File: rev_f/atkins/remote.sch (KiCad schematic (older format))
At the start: 21 parts, among them J1 Conn_01x18_Female, J11 BME390, J2 Conn_01x18_Female, J3 Conn_01x15_Female, J4 Conn_01x03_Female, J5 Conn_01x04_Female, J9 SCD30, SW1 SW_Push, SW2 SW_Push

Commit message: update
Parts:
- removed J3: Conn_01x15_Female, Connector_PinSocket_2.54mm:PinSocket_1x15_P2.54mm_Vertical, symbol Connector:Conn_01x15_Female
- added J3: Conn_01x14_Female, Connector_PinSocket_2.54mm:PinSocket_1x14_P2.54mm_Vertical, symbol Connector:Conn_01x14_Female
- added J8, J?: Conn_01x04_Female, Connector_PinSocket_2.54mm:PinSocket_1x04_P2.54mm_Vertical, symbol Connector:Conn_01x04_Female
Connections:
- net +3V3: now also J3.3 (Pin_3), J3.7 (Pin_7), J8.2 (Pin_2), J?.2 (Pin_2)
- net 34_A6: now also J3.13 (Pin_13)
- net 35_A7: now also J3.14 (Pin_14)
- net 36_A0: now also J3.9 (Pin_9)
- net 37_A1: now also J3.10 (Pin_10)
- net 38_A2: now also J3.11 (Pin_11)
- net 39_A3: now also J3.12 (Pin_12)
- net GND: now also J3.2 (Pin_2), J3.6 (Pin_6), J3.8 (Pin_8), J8.1 (Pin_1), J?.1 (Pin_1)
- net RX: now also J3.4 (Pin_4)
- net SCL: now also J8.4 (Pin_4), J?.4 (Pin_4)
- net SDA: now also J8.3 (Pin_3), J?.3 (Pin_3)
- net TX: now also J3.5 (Pin_5)
- new net VUSB: J3.1 (Pin_1)
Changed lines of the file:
@@
 Text GLabel 3150 2000 0    50   Input ~ 0
 RST
-Text GLabel 6950 3100 0    50   Input ~ 0
-SCL
-Text GLabel 6950 3200 0    50   Input ~ 0
-SDA
 Text GLabel 6950 3400 0    50   Input ~ 0
 36_A0
@@
 Text GLabel 6950 3700 0    50   Input ~ 0
 39_A3
-Text GLabel 6950 2700 0    50   Input ~ 0
+Text GLabel 6950 2900 0    50   Input ~ 0
 RX
-Text GLabel 6950 2800 0    50   Input ~ 0
+Text GLabel 6950 3000 0    50   Input ~ 0
 TX
 $Comp
@@
 L power:GND #PWR0101
 U 1 1 5FD6AB8A
-P 6675 2600
-F 0 "#PWR0101" H 6675 2350 50  0001 C CNN
-F 1 "GND" H 6680 2427 50  0000 C CNN
-F 2 "" H 6675 2600 50  0001 C CNN
-F 3 "" H 6675 2600 50  0001 C CNN
-	1    6675 2600
+P 6675 2700
+F 0 "#PWR0101" H 6675 2450 50  0001 C CNN
+F 1 "GND" H 6680 2527 50  0000 C CNN
+F 2 "" H 6675 2700 50  0001 C CNN
+F 3 "" H 6675 2700 50  0001 C CNN
+	1    6675 2700
 	0    1    1    0
 $EndComp
@@
 L power:+3V3 #PWR0105
 U 1 1 5FD6C458
-P 6950 2500
-F 0 "#PWR0105" H 6950 2350 50  0001 C CNN
-F 1 "+3V3" H 6925 2675 50  0000 C CNN
-F 2 "" H 6950 2500 50  0001 C CNN
-F 3 "" H 6950 2500 50  0001 C CNN
-	1    6950 2500
-	0    -1   -1   0
-$EndComp
-$Comp
-L power:+3V3 #PWR0106
-U 1 1 5FEF6C10
-P 6950 2900
-F 0 "#PWR0106" H 6950 2750 50  0001 C CNN
-F 1 "+3V3" H 6925 3075 50  0000 C CNN
-F 2 "" H 6950 2900 50  0001 C CNN
-F 3 "" H 6950 2900 50  0001 C CNN
-	1    6950 2900
+P 6600 2800
+F 0 "#PWR0105" H 6600 2650 50  0001 C CNN
+F 1 "+3V3" H 6575 2975 50  0000 C CNN
+F 2 "" H 6600 2800 50  0001 C CNN
+F 3 "" H 6600 2800 50  0001 C CNN
+	1    6600 2800
 	0    -1   -1   0
 $EndComp
@@
 L power:GND #PWR0117
 U 1 1 5FEF7025
-P 6675 3000
-F 0 "#PWR0117" H 6675 2750 50  0001 C CNN
-F 1 "GND" H 6680 2827 50  0000 C CNN
-F 2 "" H 6675 3000 50  0001 C CNN
-F 3 "" H 6675 3000 50  0001 C CNN
-	1    6675 3000
+P 6625 3100
+F 0 "#PWR0117" H 6625 2850 50  0001 C CNN
+F 1 "GND" H 6630 2927 50  0000 C CNN
+F 2 "" H 6625 3100 50  0001 C CNN
+F 3 "" H 6625 3100 50  0001 C CNN
+	1    6625 3100
 	0    1    1    0
-$EndComp
-Wire Wire Line
-	6950 2600 6675 2600
-Wire Wire Line
-	6950 3000 6675 3000
-$Comp
-L Connector:Conn_01x15_Female J3
-U 1 1 5FEFD935
-P 7150 3200
-F 0 "J3" H 7178 3226 50  0000 L CNN
-F 1 "Conn_01x15_Female" H 7178 3135 50  0000 L CNN
-F 2 "Connector_PinSocket_2.54mm:PinSocket_1x15_P2.54mm_Vertical" H 7150 3200 50  0001 C CNN
-F 3 "~" H 7150 3200 50  0001 C CNN
-	1    7150 3200
-	1    0    0    -1
 $EndComp
 $Comp
@@
 Wire Wire Line
 	5525 4300 5150 4300
+$Comp
+L Connector:Conn_01x04_Female J8
+U 1 1 60000D99
+P 8875 3125
+F 0 "J8" H 8903 3101 50  0000 L CNN
+F 1 "Conn_01x04_Female" H 8903 3010 50  0000 L CNN
+F 2 "Connector_PinSocket_2.54mm:PinSocket_1x04_P2.54mm_Vertical" H 8875 3125 50  0001 C CNN
+F 3 "~" H 8875 3125 50  0001 C CNN
+	1    8875 3125
+	1    0    0    -1
+$EndComp
+Text GLabel 8675 3325 0    50   Input ~ 0
+SCL
+Text GLabel 8675 3225 0    50   Input ~ 0
+SDA
+$Comp
+L power:GND #PWR0122
+U 1 1 60000DA1
+P 8300 3025
+F 0 "#PWR0122" H 8300 2775 50  0001 C CNN
+F 1 "GND" H 8305 2852 50  0000 C CNN
+F 2 "" H 8300 3025 50  0001 C CNN
+F 3 "" H 8300 3025 50  0001 C CNN
+	1    8300 3025
+	1    0    0    -1
+$EndComp
+$Comp
+L power:+3V3 #PWR0123
+U 1 1 60000DA7
+P 8550 2950
+F 0 "#PWR0123" H 8550 2800 50  0001 C CNN
+F 1 "+3V3" V 8565 3078 50  0000 L CNN
+F 2 "" H 8550 2950 50  0001 C CNN
+F 3 "" H 8550 2950 50  0001 C CNN
+	1    8550 2950
+	1    0    0    -1
+$EndComp
+Wire Wire Line
+	8675 3125 8550 3125
+Wire Wire Line
+	8550 3125 8550 2950
+Wire Wire Line
+	8675 3025 8300 3025
+Text GLabel 6950 2600 0    50   Input ~ 0
+VUSB
+$Comp
+L power:+3V3 #PWR0106
+U 1 1 6000DA3E
+P 6950 3200
+F 0 "#PWR0106" H 6950 3050 50  0001 C CNN
+F 1 "+3V3" H 6925 3375 50  0000 C CNN
+F 2 "" H 6950 3200 50  0001 C CNN
+F 3 "" H 6950 3200 50  0001 C CNN
+	1    6950 3200
+	0    -1   -1   0
+$EndComp
+$Comp
+L Connector:Conn_01x14_Female J3
+U 1 1 6003FCAE
+P 7150 3200
+F 0 "J3" H 7178 3176 50  0000 L CNN
+F 1 "Conn_01x14_Female" H 7178 3085 50  0000 L CNN
+F 2 "Connector_PinSocket_2.54mm:PinSocket_1x14_P2.54mm_Vertical" H 7150 3200 50  0001 C CNN
+F 3 "~" H 7150 3200 50  0001 C CNN
+	1    7150 3200
+	1    0    0    -1
+$EndComp
+Wire Wire Line
+	6950 2700 6675 2700
+Wire Wire Line
+	6950 2800 6600 2800
+Wire Wire Line
+	6950 3100 6625 3100
+$Comp
+L Connector:Conn_01x04_Female J?
+U 1 1 60065C2D
+P 9450 2200
+F 0 "J?" H 9478 2176 50  0000 L CNN
+F 1 "Conn_01x04_Female" H 9478 2085 50  0000 L CNN
+F 2 "Connector_PinSocket_2.54mm:PinSocket_1x04_P2.54mm_Vertical" H 9450 2200 50  0001 C CNN
+F 3 "~" H 9450 2200 50  0001 C CNN
+	1    9450 2200
+	1    0    0    -1
+$EndComp
+Text GLabel 9250 2400 0    50   Input ~ 0
+SCL
+Text GLabel 9250 2300 0    50   Input ~ 0
+SDA
+$Comp
+L power:GND #PWR?
+U 1 1 60065C39
+P 8875 2100
+F 0 "#PWR?" H 8875 1850 50  0001 C CNN
+F 1 "GND" H 8880 1927 50  0000 C CNN
+F 2 "" H 8875 2100 50  0001 C CNN
+F 3 "" H 8875 2100 50  0001 C CNN
+	1    8875 2100
+	1    0    0    -1
+$EndComp
+$Comp
+L power:+3V3 #PWR?
+U 1 1 60065C43
+P 9125 2025
+F 0 "#PWR?" H 9125 1875 50  0001 C CNN
+F 1 "+3V3" V 9140 2153 50  0000 L CNN
+F 2 "" H 9125 2025 50  0001 C CNN
+F 3 "" H 9125 2025 50  0001 C CNN
+	1    9125 2025
+	1    0    0    -1
+$EndComp
+Wire Wire Line
+	9250 2200 9125 2200
+Wire Wire Line
+	9125 2200 9125 2025
+Wire Wire Line
+	9250 2100 8875 2100
 $EndSCHEMATC

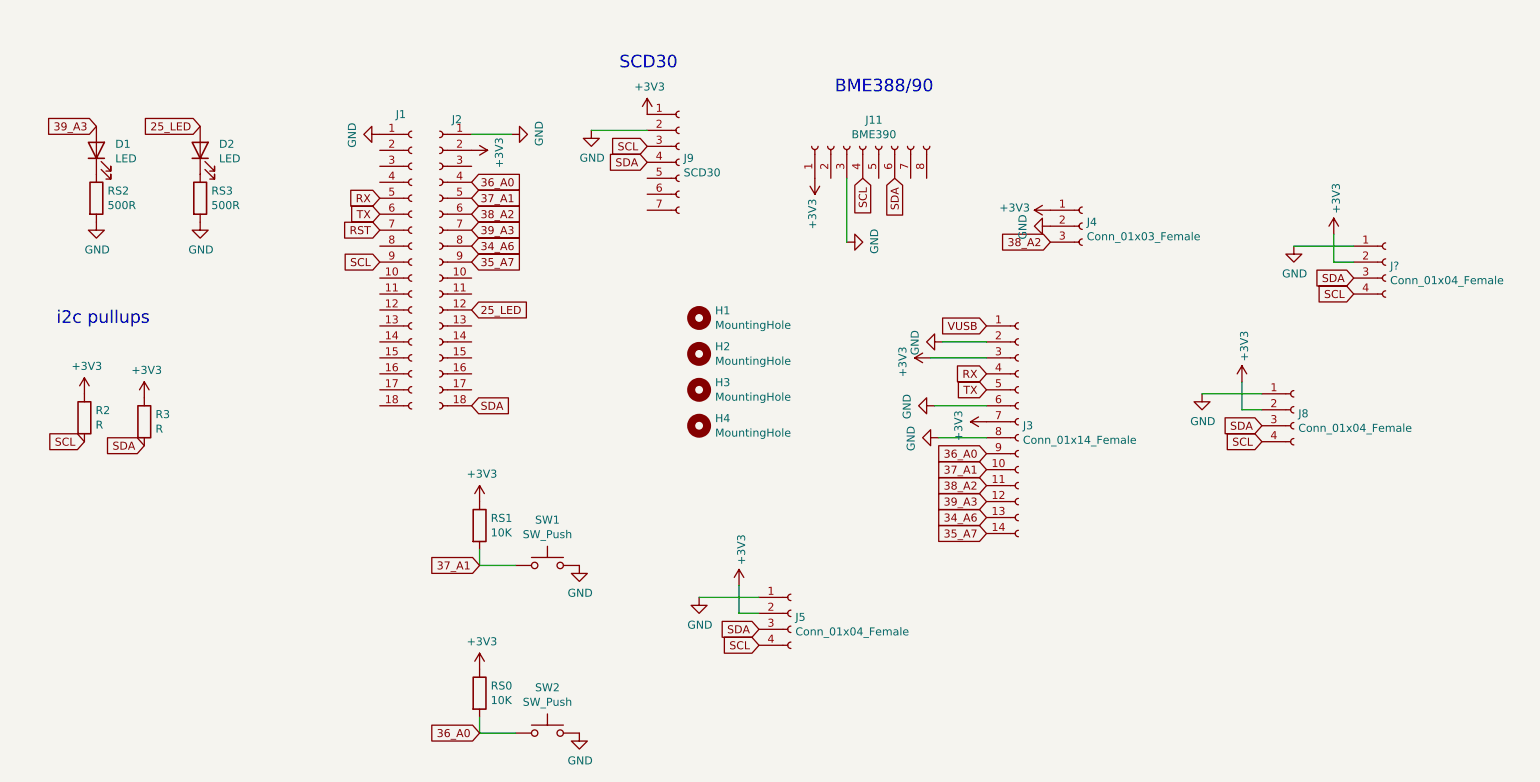
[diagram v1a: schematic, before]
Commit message: fully routed
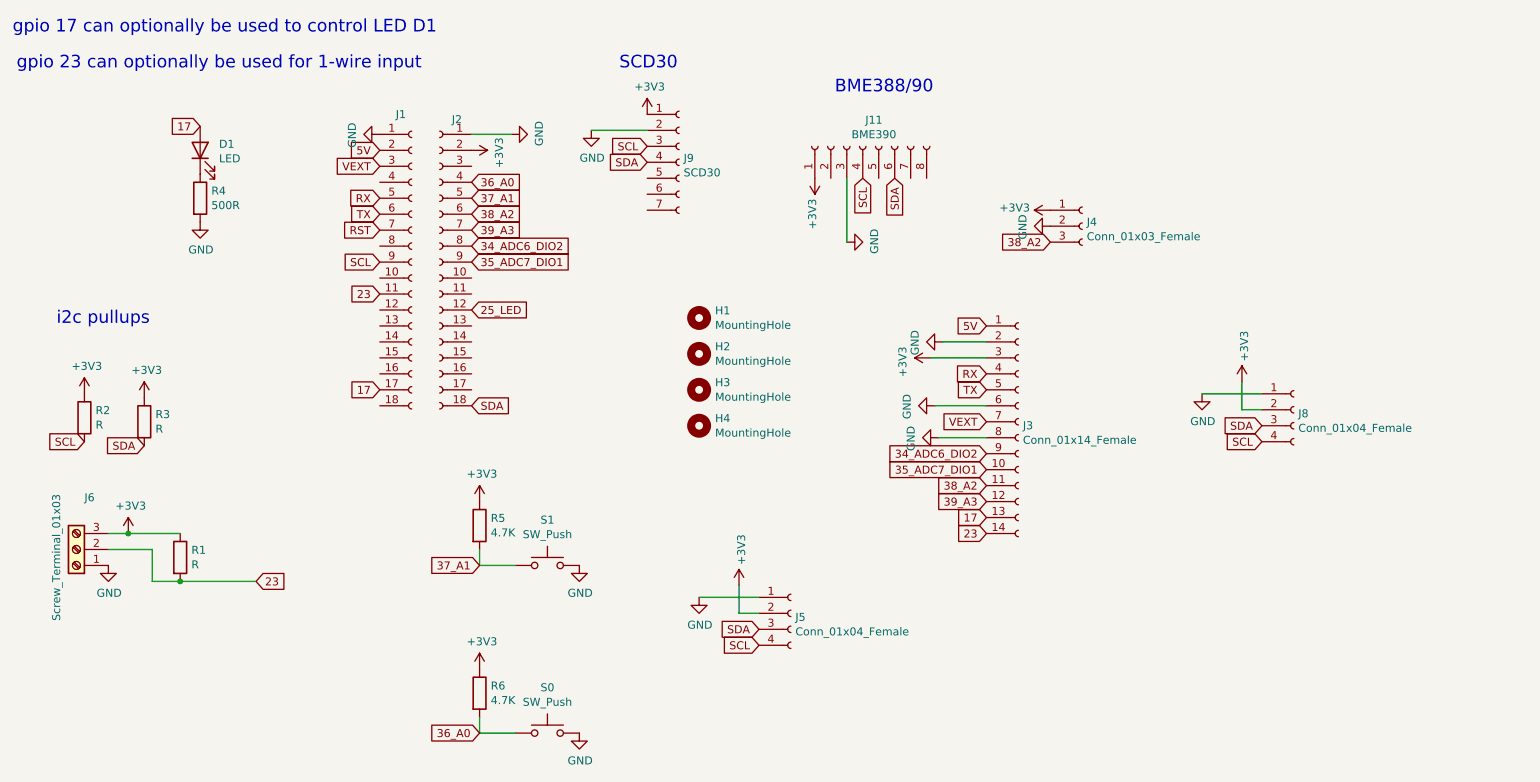
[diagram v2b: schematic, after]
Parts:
- removed D1: LED, LED_THT:LED_D5.0mm, symbol Device:LED
- removed J?: Conn_01x04_Female, Connector_PinSocket_2.54mm:PinSocket_1x04_P2.54mm_Vertical, symbol Connector:Conn_01x04_Female
- removed RS2: 500R, Resistor_THT:R_Axial_DIN0207_L6.3mm_D2.5mm_P10.16mm_Horizontal, symbol Device:R
- added J6: Screw_Terminal_01x03, TerminalBlock_Phoenix:TerminalBlock_Phoenix_PT-1,5-3-3.5-H_1x03_P3.50mm_Horizontal, symbol Connector:Screw_Terminal_01x03
- added R1: R, Resistor_THT:R_Axial_DIN0207_L6.3mm_D2.5mm_P10.16mm_Horizontal, symbol Device:R
- R5: renamed from RS1; value 10K -> 4.7K
- R6: renamed from RS0; value 10K -> 4.7K
- renumbered D2 to D1, RS3 to R4, SW2 to S0, SW1 to S1
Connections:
- net VUSB is gone; now on net 5V: J3.1 (Pin_1)
- net +3V3: now also J6.3 (Pin_3), R1.1; no longer J3.7 (Pin_7)
- net 25_LED: no longer D1.2 (A)
- net 36_A0: no longer J3.9 (Pin_9)
- net 37_A1: no longer J3.10 (Pin_10)
- net GND: now also J6.1 (Pin_1)
- net 23: now reaches J1.11 (Pin_11)
- net 23: now also J3.14 (Pin_14), J6.2 (Pin_2), R1.2
- net 17: now reaches J1.17 (Pin_17)
- net 17: now also D1.2 (A), J3.13 (Pin_13)
- net 5V: now reaches J1.2 (Pin_2)
- net VEXT: now reaches J1.3 (Pin_3)
- net VEXT: now also J3.7 (Pin_7)
- net 34_A6 renamed 34_ADC6_DIO2
- net 34_ADC6_DIO2: now also J3.9 (Pin_9); no longer J3.13 (Pin_13)
- net 35_A7 renamed 35_ADC7_DIO1
- net 35_ADC7_DIO1: now also J3.10 (Pin_10); no longer J3.14 (Pin_14)
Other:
- note added: "gpio 17 can optionally be used to control LED D1"
- note added: "gpio 23 can optionally be used for 1-wire input"
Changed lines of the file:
@@
 Text Notes 6000 1150 0    79   ~ 0
 BME388/90
-Text GLabel 3775 4100 0    50   Input ~ 0
-37_A1
 $Comp
 L power:+3V3 #PWR0134
@@
 $EndComp
 $Comp
-L Device:R RS1
+L Device:R R5
 U 1 1 5FBA6976
 P 3775 3850
-F 0 "RS1" H 3845 3896 50  0000 L CNN
-F 1 "10K" H 3845 3805 50  0000 L CNN
+F 0 "R5" H 3845 3896 50  0000 L CNN
+F 1 "4.7K" H 3845 3805 50  0000 L CNN
 F 2 "Resistor_THT:R_Axial_DIN0207_L6.3mm_D2.5mm_P10.16mm_Horizontal" V 3705 3850 50  0001 C CNN
 F 3 "~" H 3775 3850 50  0001 C CNN
@@
 Wire Wire Line
 	4000 4100 3775 4100
-Text GLabel 3775 5150 0    50   Input ~ 0
-36_A0
 $Comp
 L power:+3V3 #PWR0136
@@
 $EndComp
 $Comp
-L Device:R RS0
+L Device:R R6
 U 1 1 5FBA90BC
 P 3775 4900
-F 0 "RS0" H 3845 4946 50  0000 L CNN
-F 1 "10K" H 3845 4855 50  0000 L CNN
+F 0 "R6" H 3845 4946 50  0000 L CNN
+F 1 "4.7K" H 3845 4855 50  0000 L CNN
 F 2 "Resistor_THT:R_Axial_DIN0207_L6.3mm_D2.5mm_P10.16mm_Horizontal" V 3705 4900 50  0001 C CNN
 F 3 "~" H 3775 4900 50  0001 C CNN
@@
 Text GLabel 3150 2000 0    50   Input ~ 0
 RST
-Text GLabel 6950 3400 0    50   Input ~ 0
-36_A0
-Text GLabel 6950 3500 0    50   Input ~ 0
-37_A1
 Text GLabel 6950 3600 0    50   Input ~ 0
 38_A2
-Text GLabel 6950 3700 0    50   Input ~ 0
-39_A3
 Text GLabel 6950 2900 0    50   Input ~ 0
 RX
@@
 $EndComp
 $Comp
-L Device:R RS2
-U 1 1 5FDD33D4
-P 1375 1800
-F 0 "RS2" H 1445 1846 50  0000 L CNN
-F 1 "500R" H 1445 1755 50  0000 L CNN
-F 2 "Resistor_THT:R_Axial_DIN0207_L6.3mm_D2.5mm_P10.16mm_Horizontal" V 1305 1800 50  0001 C CNN
-F 3 "~" H 1375 1800 50  0001 C CNN
-	1    1375 1800
-	1    0    0    -1
-$EndComp
-$Comp
-L power:GND #PWR0108
-U 1 1 5FDD364E
-P 1375 1950
-F 0 "#PWR0108" H 1375 1700 50  0001 C CNN
-F 1 "GND" H 1380 1777 50  0000 C CNN
-F 2 "" H 1375 1950 50  0001 C CNN
-F 3 "" H 1375 1950 50  0001 C CNN
-	1    1375 1950
-	1    0    0    -1
-$EndComp
-Text GLabel 1375 1350 0    50   Input ~ 0
-39_A3
-$Comp
-L Device:LED D1
-U 1 1 5FDEF6AE
-P 1375 1500
-F 0 "D1" V 1414 1382 50  0000 R CNN
-F 1 "LED" V 1323 1382 50  0000 R CNN
-F 2 "LED_THT:LED_D5.0mm" H 1375 1500 50  0001 C CNN
-F 3 "~" H 1375 1500 50  0001 C CNN
-	1    1375 1500
-	0    -1   -1   0
-$EndComp
-$Comp
 L Mechanical:MountingHole H1
 U 1 1 5FDF5FDF
@@
 Text GLabel 3725 2500 2    50   Input ~ 0
 25_LED
-Text GLabel 3725 2100 2    50   Input ~ 0
-34_A6
-Text GLabel 3725 2200 2    50   Input ~ 0
-35_A7
-Text GLabel 6950 3800 0    50   Input ~ 0
-34_A6
-Text GLabel 6950 3900 0    50   Input ~ 0
-35_A7
 $Comp
 L Connector:Conn_01x04_Female J5
@@
 $EndComp
 $Comp
-L Device:R RS3
+L Device:R R4
 U 1 1 5FE7DEE6
 P 2025 1800
-F 0 "RS3" H 2095 1846 50  0000 L CNN
+F 0 "R4" H 2095 1846 50  0000 L CNN
 F 1 "500R" H 2095 1755 50  0000 L CNN
 F 2 "Resistor_THT:R_Axial_DIN0207_L6.3mm_D2.5mm_P10.16mm_Horizontal" V 1955 1800 50  0001 C CNN
@@
 $EndComp
 $Comp
-L Device:LED D2
+L Device:LED D1
 U 1 1 5FE7DEFB
 P 2025 1500
-F 0 "D2" V 2064 1382 50  0000 R CNN
+F 0 "D1" V 2064 1382 50  0000 R CNN
 F 1 "LED" V 1973 1382 50  0000 R CNN
 F 2 "LED_THT:LED_D5.0mm" H 2025 1500 50  0001 C CNN
@@
 	0    -1   -1   0
 $EndComp
-Text GLabel 2025 1350 0    50   Input ~ 0
-25_LED
 Text GLabel 7350 2075 0    50   Input ~ 0
 38_A2
@@
 $EndComp
 $Comp
-L Switch:SW_Push SW1
+L Switch:SW_Push S1
 U 1 1 5FDA65F7
 P 4200 4100
-F 0 "SW1" H 4200 4385 50  0000 C CNN
+F 0 "S1" H 4200 4385 50  0000 C CNN
 F 1 "SW_Push" H 4200 4294 50  0000 C CNN
 F 2 "Button_Switch_THT:SW_Tactile_SPST_Angled_PTS645Vx58-2LFS" H 4200 4300 50  0001 C CNN
@@
 $EndComp
 $Comp
-L Switch:SW_Push SW2
+L Switch:SW_Push S0
 U 1 1 5FDC768B
 P 4200 5150
-F 0 "SW2" H 4200 5435 50  0000 C CNN
+F 0 "S0" H 4200 5435 50  0000 C CNN
 F 1 "SW_Push" H 4200 5344 50  0000 C CNN
 F 2 "Button_Switch_THT:SW_Tactile_SPST_Angled_PTS645Vx58-2LFS" H 4200 5350 50  0001 C CNN
@@
 Wire Wire Line
 	8675 3025 8300 3025
-Text GLabel 6950 2600 0    50   Input ~ 0
-VUSB
-$Comp
-L power:+3V3 #PWR0106
-U 1 1 6000DA3E
-P 6950 3200
-F 0 "#PWR0106" H 6950 3050 50  0001 C CNN
-F 1 "+3V3" H 6925 3375 50  0000 C CNN
-F 2 "" H 6950 3200 50  0001 C CNN
-F 3 "" H 6950 3200 50  0001 C CNN
-	1    6950 3200
-	0    -1   -1   0
-$EndComp
 $Comp
 L Connector:Conn_01x14_Female J3
@@
 Wire Wire Line
 	6950 3100 6625 3100
-$Comp
-L Connector:Conn_01x04_Female J?
-U 1 1 60065C2D
-P 9450 2200
-F 0 "J?" H 9478 2176 50  0000 L CNN
-F 1 "Conn_01x04_Female" H 9478 2085 50  0000 L CNN
-F 2 "Connector_PinSocket_2.54mm:PinSocket_1x04_P2.54mm_Vertical" H 9450 2200 50  0001 C CNN
-F 3 "~" H 9450 2200 50  0001 C CNN
-	1    9450 2200
-	1    0    0    -1
-$EndComp
-Text GLabel 9250 2400 0    50   Input ~ 0
-SCL
-Text GLabel 9250 2300 0    50   Input ~ 0
-SDA
-$Comp
-L power:GND #PWR?
-U 1 1 60065C39
-P 8875 2100
-F 0 "#PWR?" H 8875 1850 50  0001 C CNN
-F 1 "GND" H 8880 1927 50  0000 C CNN
-F 2 "" H 8875 2100 50  0001 C CNN
-F 3 "" H 8875 2100 50  0001 C CNN
-	1    8875 2100
-	1    0    0    -1
-$EndComp
-$Comp
-L power:+3V3 #PWR?
-U 1 1 60065C43
-P 9125 2025
-F 0 "#PWR?" H 9125 1875 50  0001 C CNN
-F 1 "+3V3" V 9140 2153 50  0000 L CNN
-F 2 "" H 9125 2025 50  0001 C CNN
-F 3 "" H 9125 2025 50  0001 C CNN
-	1    9125 2025
-	1    0    0    -1
-$EndComp
-Wire Wire Line
-	9250 2200 9125 2200
-Wire Wire Line
-	9125 2200 9125 2025
-Wire Wire Line
-	9250 2100 8875 2100
+Text GLabel 3150 1500 0    50   Input ~ 0
+5V
+Text GLabel 6950 2600 0    50   Input ~ 0
+5V
+Text GLabel 3150 1600 0    50   Input ~ 0
+VEXT
+Text GLabel 6950 3200 0    50   Input ~ 0
+VEXT
+Text GLabel 3150 3000 0    50   Input ~ 0
+17
+Text GLabel 3150 2400 0    50   Input ~ 0
+23
+Text GLabel 6950 3700 0    50   Input ~ 0
+39_A3
+Text GLabel 6950 3800 0    50   Input ~ 0
+17
+Text GLabel 6950 3900 0    50   Input ~ 0
+23
+Text GLabel 2025 1350 0    50   Input ~ 0
+17
+Text GLabel 3775 5150 0    50   Input ~ 0
+36_A0
+Text GLabel 3775 4100 0    50   Input ~ 0
+37_A1
+Text GLabel 3725 2200 2    50   Input ~ 0
+35_ADC7_DIO1
+Text GLabel 3725 2100 2    50   Input ~ 0
+34_ADC6_DIO2
+Text GLabel 6950 3400 0    50   Input ~ 0
+34_ADC6_DIO2
+Text GLabel 6950 3500 0    50   Input ~ 0
+35_ADC7_DIO1
+$Comp
+L Connector:Screw_Terminal_01x03 J6
+U 1 1 601266D8
+P 1250 4000
+F 0 "J6" H 1168 3675 50  0000 C CNN
+F 1 "Screw_Terminal_01x03" V 1375 4050 50  0000 C CNN
+F 2 "TerminalBlock_Phoenix:TerminalBlock_Phoenix_PT-1,5-3-3.5-H_1x03_P3.50mm_Horizontal" H 1250 4000 50  0001 C CNN
+F 3 "~" H 1250 4000 50  0001 C CNN
+	1    1250 4000
+	-1   0    0    1
+$EndComp
+$Comp
+L power:GND #PWR0106
+U 1 1 601270CB
+P 1450 4100
+F 0 "#PWR0106" H 1450 3850 50  0001 C CNN
+F 1 "GND" H 1455 3927 50  0000 C CNN
+F 2 "" H 1450 4100 50  0001 C CNN
+F 3 "" H 1450 4100 50  0001 C CNN
+	1    1450 4100
+	1    0    0    -1
+$EndComp
+$Comp
+L Device:R R1
+U 1 1 601290C7
+P 1900 4050
+F 0 "R1" H 1970 4096 50  0000 L CNN
+F 1 "R" H 1970 4005 50  0000 L CNN
+F 2 "Resistor_THT:R_Axial_DIN0207_L6.3mm_D2.5mm_P10.16mm_Horizontal" V 1830 4050 50  0001 C CNN
+F 3 "~" H 1900 4050 50  0001 C CNN
+	1    1900 4050
+	1    0    0    -1
+$EndComp
+Wire Wire Line
+	1450 3900 1575 3900
+Wire Wire Line
+	1450 4000 1725 4000
+Wire Wire Line
+	1725 4000 1725 4200
+Wire Wire Line
+	1725 4200 1900 4200
+$Comp
+L power:+3V3 #PWR0108
+U 1 1 6012ADEB
+P 1575 3900
+F 0 "#PWR0108" H 1575 3750 50  0001 C CNN
+F 1 "+3V3" H 1590 4073 50  0000 C CNN
+F 2 "" H 1575 3900 50  0001 C CNN
+F 3 "" H 1575 3900 50  0001 C CNN
+	1    1575 3900
+	1    0    0    -1
+$EndComp
+Connection ~ 1575 3900
+Wire Wire Line
+	1575 3900 1900 3900
+Wire Wire Line
+	1900 4200 2375 4200
+Connection ~ 1900 4200
+Text GLabel 2375 4200 2    50   Input ~ 0
+23
+Text Notes 850  775  0    79   ~ 0
+gpio 17 can optionally be used to control LED D1
+Text Notes 875  1000 0    79   ~ 0
+gpio 23 can optionally be used for 1-wire input
 $EndSCHEMATC
